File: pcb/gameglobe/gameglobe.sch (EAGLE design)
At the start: 14 parts

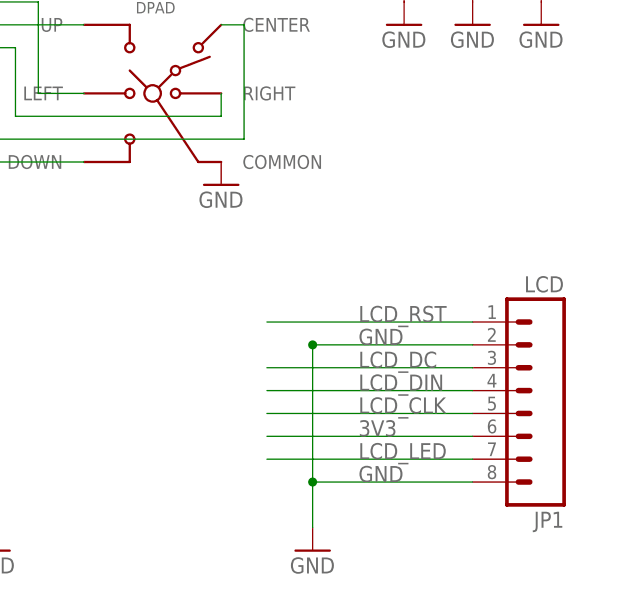
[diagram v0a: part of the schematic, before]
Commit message: Improved silkscreen
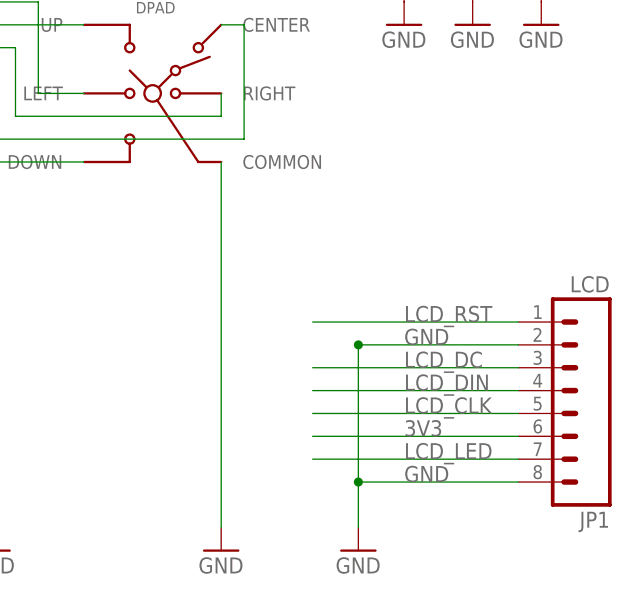
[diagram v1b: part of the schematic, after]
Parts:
- JP1: device SparkFun-Connectors:M08NO_SILK -> SparkFun-Connectors:M08
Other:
- moved on the sheet: JP1
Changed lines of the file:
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@@
 <part name="GND1" library="supply1" deviceset="GND" device=""/>
 <part name="GND2" library="supply1" deviceset="GND" device=""/>
-<part name="JP1" library="SparkFun-Connectors" deviceset="M08" device="NO_SILK" value="LCD"/>
+<part name="JP1" library="SparkFun-Connectors" deviceset="M08" device="" value="LCD"/>
 <part name="GND3" library="supply1" deviceset="GND" device=""/>
 <part name="GND4" library="supply1" deviceset="GND" device=""/>
@@
 <instance part="GND1" gate="1" x="96.52" y="0"/>
 <instance part="GND2" gate="1" x="15.24" y="0"/>
-<instance part="JP1" gate="G$1" x="154.94" y="17.78" rot="R180"/>
-<instance part="GND3" gate="1" x="132.08" y="0"/>
+<instance part="JP1" gate="G$1" x="160.02" y="17.78" rot="R180"/>
+<instance part="GND3" gate="1" x="137.16" y="0"/>
 <instance part="GND4" gate="1" x="15.24" y="58.42"/>
 <instance part="GND5" gate="1" x="142.24" y="58.42"/>
@@
 <instance part="GND7" gate="1" x="157.48" y="58.42"/>
 <instance part="DPAD" gate="Q$1" x="114.3" y="50.8"/>
-<instance part="GND8" gate="1" x="121.92" y="40.64"/>
+<instance part="GND8" gate="1" x="121.92" y="0"/>
 <instance part="R1" gate="G$1" x="20.32" y="30.48"/>
 <instance part="ARDUINO_NANO" gate="G$1" x="66.04" y="12.7" rot="R180"/>
@@
 </segment>
 <segment>
-<wire x1="132.08" y1="22.86" x2="132.08" y2="7.62" width="0.1524" layer="91"/>
+<wire x1="137.16" y1="22.86" x2="137.16" y2="7.62" width="0.1524" layer="91"/>
 <pinref part="JP1" gate="G$1" pin="8"/>
-<wire x1="149.86" y1="7.62" x2="132.08" y2="7.62" width="0.1524" layer="91"/>
-<label x="137.16" y="7.62" size="1.778" layer="95"/>
+<wire x1="154.94" y1="7.62" x2="137.16" y2="7.62" width="0.1524" layer="91"/>
+<label x="142.24" y="7.62" size="1.778" layer="95"/>
 <pinref part="JP1" gate="G$1" pin="2"/>
-<wire x1="149.86" y1="22.86" x2="132.08" y2="22.86" width="0.1524" layer="91"/>
-<label x="137.16" y="22.86" size="1.778" layer="95"/>
-<junction x="132.08" y="22.86"/>
+<wire x1="154.94" y1="22.86" x2="137.16" y2="22.86" width="0.1524" layer="91"/>
+<label x="142.24" y="22.86" size="1.778" layer="95"/>
+<junction x="137.16" y="22.86"/>
 <pinref part="GND3" gate="1" pin="GND"/>
-<wire x1="132.08" y1="7.62" x2="132.08" y2="2.54" width="0.1524" layer="91"/>
-<junction x="132.08" y="7.62"/>
+<wire x1="137.16" y1="7.62" x2="137.16" y2="2.54" width="0.1524" layer="91"/>
+<junction x="137.16" y="7.62"/>
 </segment>
 <segment>
@@
 <pinref part="DPAD" gate="Q$1" pin="COMMON"/>
 <pinref part="GND8" gate="1" pin="GND"/>
+<wire x1="121.92" y1="2.54" x2="121.92" y2="43.18" width="0.1524" layer="91"/>
 </segment>
 </net>
@@
 <segment>
 <pinref part="JP1" gate="G$1" pin="1"/>
-<wire x1="149.86" y1="25.4" x2="127" y2="25.4" width="0.1524" layer="91"/>
-<label x="137.16" y="25.4" size="1.778" layer="95"/>
+<wire x1="154.94" y1="25.4" x2="132.08" y2="25.4" width="0.1524" layer="91"/>
+<label x="142.24" y="25.4" size="1.778" layer="95"/>
 </segment>
 <segment>
@@
 <segment>
 <pinref part="JP1" gate="G$1" pin="3"/>
-<wire x1="149.86" y1="20.32" x2="127" y2="20.32" width="0.1524" layer="91"/>
-<label x="137.16" y="20.32" size="1.778" layer="95"/>
+<wire x1="154.94" y1="20.32" x2="132.08" y2="20.32" width="0.1524" layer="91"/>
+<label x="142.24" y="20.32" size="1.778" layer="95"/>
 </segment>
 <segment>
@@
 <segment>
 <pinref part="JP1" gate="G$1" pin="4"/>
-<wire x1="149.86" y1="17.78" x2="127" y2="17.78" width="0.1524" layer="91"/>
-<label x="137.16" y="17.78" size="1.778" layer="95"/>
+<wire x1="154.94" y1="17.78" x2="132.08" y2="17.78" width="0.1524" layer="91"/>
+<label x="142.24" y="17.78" size="1.778" layer="95"/>
 </segment>
 <segment>
@@
 <segment>
 <pinref part="JP1" gate="G$1" pin="5"/>
-<wire x1="149.86" y1="15.24" x2="127" y2="15.24" width="0.1524" layer="91"/>
-<label x="137.16" y="15.24" size="1.778" layer="95"/>
+<wire x1="154.94" y1="15.24" x2="132.08" y2="15.24" width="0.1524" layer="91"/>
+<label x="142.24" y="15.24" size="1.778" layer="95"/>
 </segment>
 <segment>
@@
 <segment>
 <pinref part="JP1" gate="G$1" pin="6"/>
-<wire x1="149.86" y1="12.7" x2="127" y2="12.7" width="0.1524" layer="91"/>
-<label x="137.16" y="12.7" size="1.778" layer="95"/>
+<wire x1="154.94" y1="12.7" x2="132.08" y2="12.7" width="0.1524" layer="91"/>
+<label x="142.24" y="12.7" size="1.778" layer="95"/>
 </segment>
 <segment>
@@
 <segment>
 <pinref part="JP1" gate="G$1" pin="7"/>
-<wire x1="149.86" y1="10.16" x2="127" y2="10.16" width="0.1524" layer="91"/>
-<label x="137.16" y="10.16" size="1.778" layer="95"/>
+<wire x1="154.94" y1="10.16" x2="132.08" y2="10.16" width="0.1524" layer="91"/>
+<label x="142.24" y="10.16" size="1.778" layer="95"/>
 </segment>
 <segment>

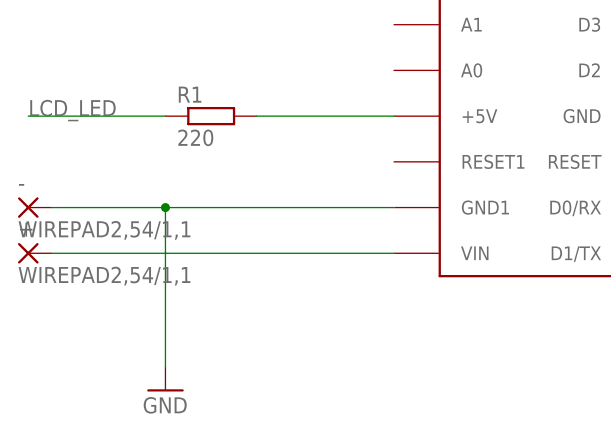
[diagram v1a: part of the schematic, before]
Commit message: Added power switch to pcb. LCD pin labels on slikscreen
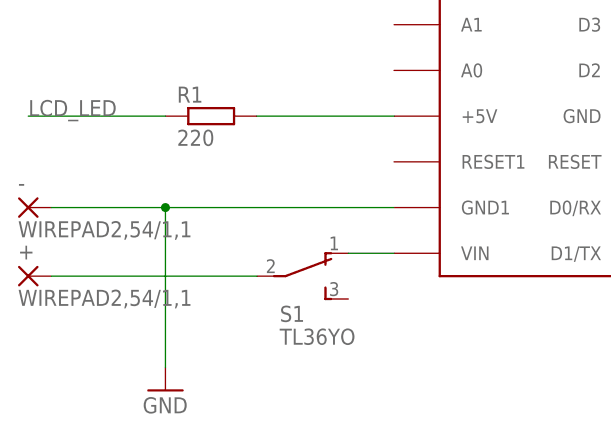
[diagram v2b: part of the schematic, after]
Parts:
- added S1: TL36YO, switch:TL36YO
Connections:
- removed net N$7: +.P, ARDUINO_NANO.VIN
- new net N$5: ARDUINO_NANO.VIN, S1.O
- new net N$6: +.P, S1.P
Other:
- moved on the sheet: +
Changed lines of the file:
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@@
 <part name="R1" library="resistor" deviceset="R-EU_" device="0411/15" value="220"/>
 <part name="ARDUINO_NANO" library="arduino_nano" deviceset="ARDUINONANO" device=""/>
+<part name="S1" library="switch" deviceset="TL36YO" device=""/>
 </parts>
 <sheets>
@@
 </plain>
 <instances>
-<instance part="+" gate="G$1" x="0" y="15.24"/>
+<instance part="+" gate="G$1" x="0" y="12.7"/>
 <instance part="-" gate="G$1" x="0" y="20.32"/>
 <instance part="R5" gate="G$1" x="22.86" y="86.36"/>
@@
 <instance part="R1" gate="G$1" x="20.32" y="30.48"/>
 <instance part="ARDUINO_NANO" gate="G$1" x="66.04" y="12.7" rot="R180"/>
+<instance part="S1" gate="BEF1" x="30.48" y="12.7" rot="R270"/>
 </instances>
 <busses>
 </busses>
 <nets>
-<net name="N$7" class="0">
-<segment>
-<pinref part="+" gate="G$1" pin="P"/>
-<wire x1="40.64" y1="15.24" x2="2.54" y2="15.24" width="0.1524" layer="91"/>
-<pinref part="ARDUINO_NANO" gate="G$1" pin="VIN"/>
-</segment>
-</net>
 <net name="GND" class="0">
 <segment>
@@
 </segment>
 </net>
+<net name="N$5" class="0">
+<segment>
+<pinref part="ARDUINO_NANO" gate="G$1" pin="VIN"/>
+<pinref part="S1" gate="BEF1" pin="O"/>
+<wire x1="40.64" y1="15.24" x2="35.56" y2="15.24" width="0.1524" layer="91"/>
+</segment>
+</net>
+<net name="N$6" class="0">
+<segment>
+<pinref part="S1" gate="BEF1" pin="P"/>
+<pinref part="+" gate="G$1" pin="P"/>
+<wire x1="25.4" y1="12.7" x2="2.54" y2="12.7" width="0.1524" layer="91"/>
+</segment>
+</net>

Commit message: Set LED resistor value to 100 (after testing with prototype); Move some silkscreen items around; Enable all needed layers in Eagle
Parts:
- R1: value 220 -> 100
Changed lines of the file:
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@@
 <part name="DPAD" library="gamaral" deviceset="SKQU" device="CAA010"/>
 <part name="GND8" library="supply1" deviceset="GND" device=""/>
-<part name="R1" library="resistor" deviceset="R-EU_" device="0411/15" value="220"/>
+<part name="R1" library="resistor" deviceset="R-EU_" device="0411/15" value="100"/>
 <part name="ARDUINO_NANO" library="arduino_nano" deviceset="ARDUINONANO" device=""/>
 <part name="S1" library="switch" deviceset="TL36YO" device=""/>

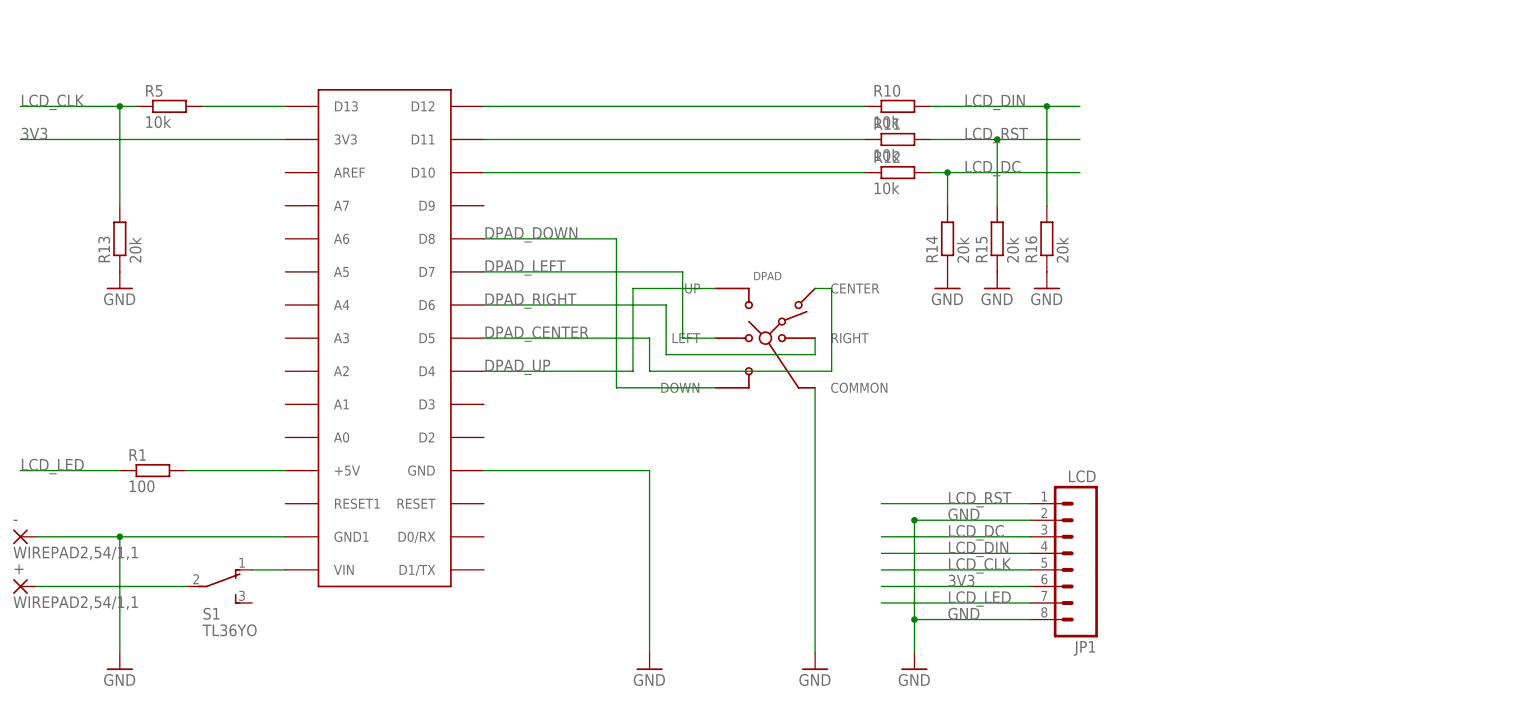
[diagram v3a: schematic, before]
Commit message: Changed to cheaper speaker (flat piezo buzzer); Mount speaker belof display, add connector for speaker; Improve 9V connector; Improve silkscreen again;
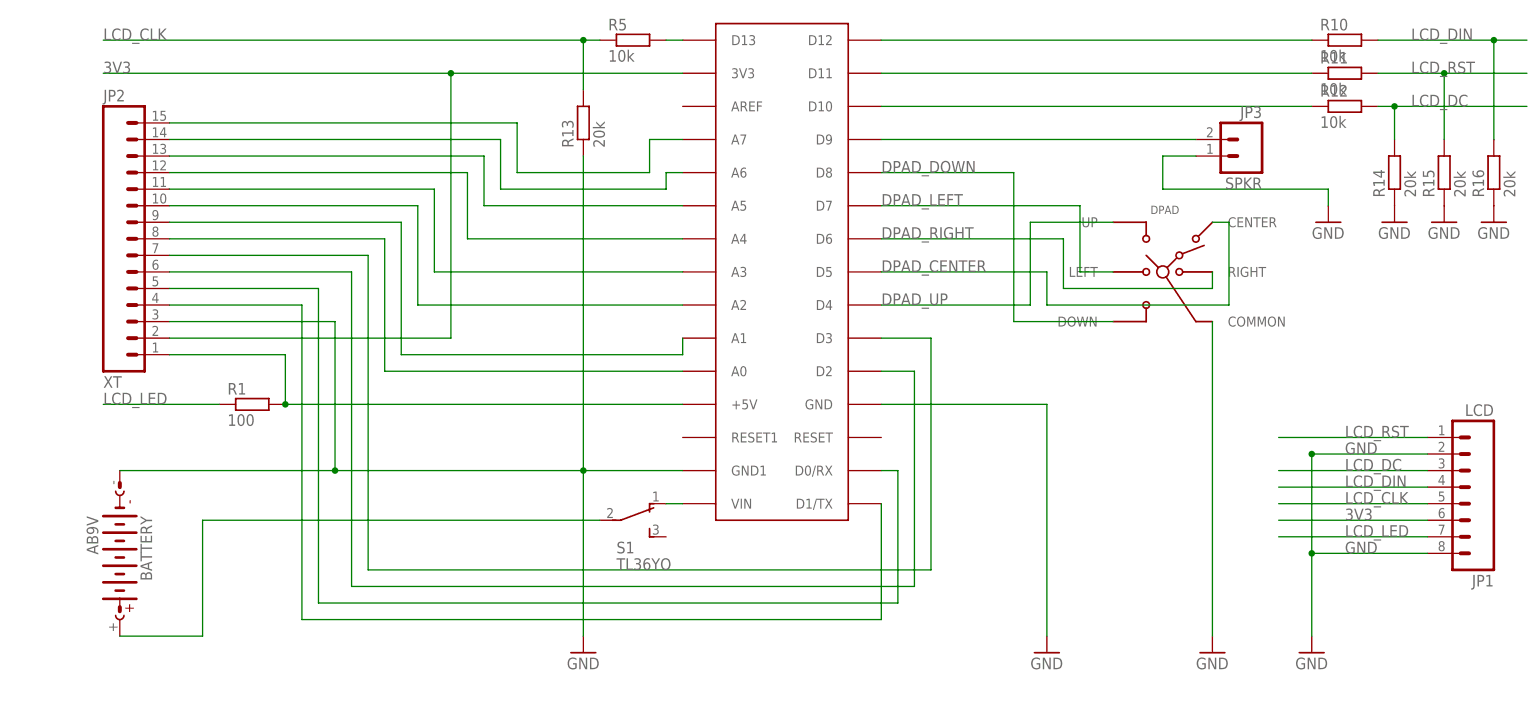
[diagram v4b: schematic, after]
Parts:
- removed +, -: WIREPAD2,54/1,1, wirepad:WIREPAD2,54/1,1
- added BATTERY: AB9V, battery:AB9V
- added JP2: XT, SparkFun-Connectors:M15
- added JP3: SPKR, SparkFun-Connectors:M02PTH
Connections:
- new net N$11: ARDUINO_NANO.A0, JP2.8
- new net N$12: ARDUINO_NANO.A1, JP2.9
- new net N$13: ARDUINO_NANO.A2, JP2.10
- new net N$14: ARDUINO_NANO.A3, JP2.11
- new net N$15: ARDUINO_NANO.A4, JP2.12
- new net N$16: ARDUINO_NANO.A5, JP2.13
- new net N$17: ARDUINO_NANO.A6, JP2.14
- new net N$18: ARDUINO_NANO.A7, JP2.15
- new net N$19: ARDUINO_NANO.D3, JP2.7
- new net N$7: ARDUINO_NANO.D1/TX, JP2.4
- new net N$8: ARDUINO_NANO.D0/RX, JP2.5
- new net N$9: ARDUINO_NANO.D2, JP2.6
- new net SPKR: ARDUINO_NANO.D9, JP3.2
- net 3V3: now also JP2.2
- net 5V: now also JP2.1
- net GND: now also BATTERY.-, JP2.3, JP3.1; no longer -.P
- net N$6: now also BATTERY.+; no longer +.P
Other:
- moved on the sheet: DPAD, JP1, R1, R10, R11, R12, R13, R14, R15, R16, R5, S1

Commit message: change wiring to use different pins for the speaker with ToneAC library (and also all the buttons)
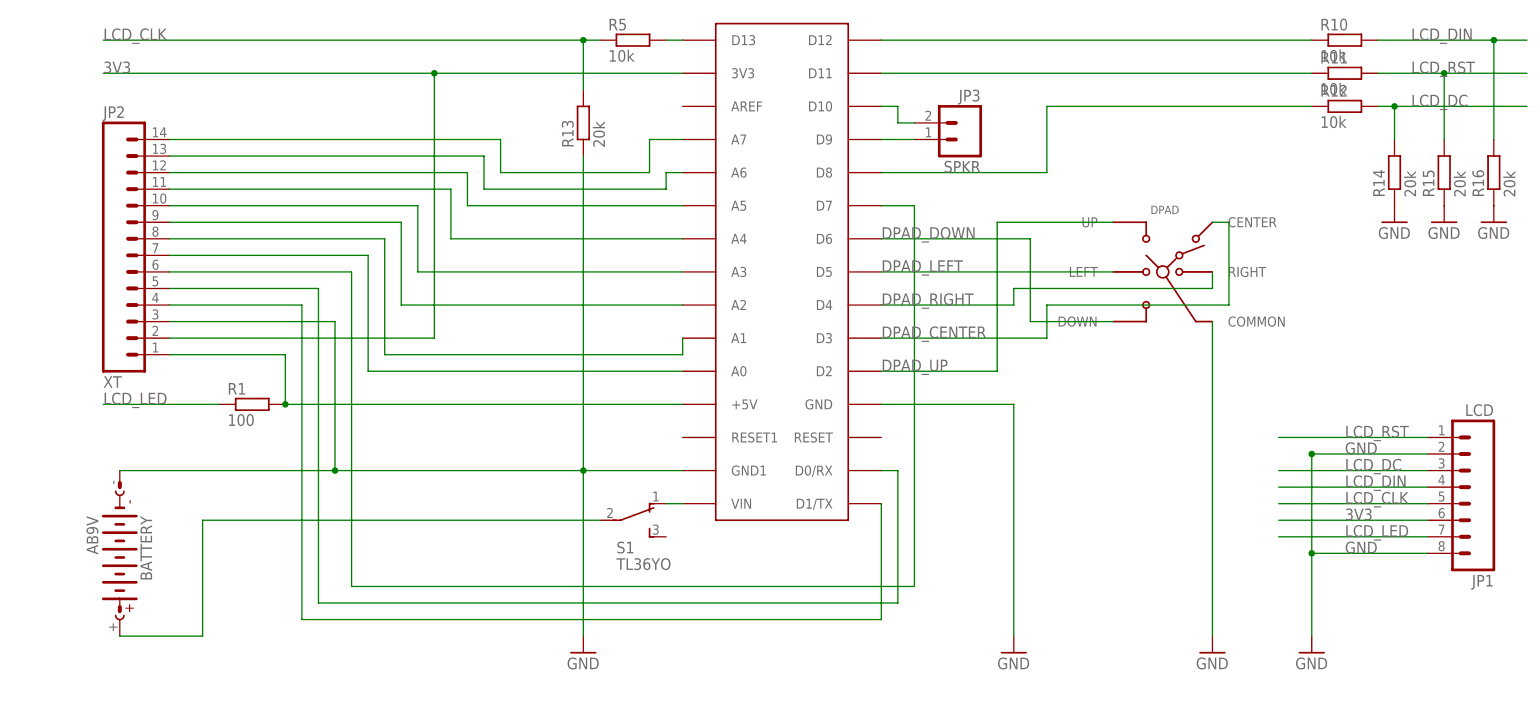
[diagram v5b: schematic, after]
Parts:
- JP2: device SparkFun-Connectors:M15 -> SparkFun-Connectors:M14LONGPADS
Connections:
- removed net N$19: ARDUINO_NANO.D3, JP2.7
- removed net SPKR: ARDUINO_NANO.D9, JP3.2
- new net N$10: ARDUINO_NANO.D10, JP3.2
- new net N$20: ARDUINO_NANO.D8, R12.1
- net DPAD_CENTER: now also ARDUINO_NANO.D3; no longer ARDUINO_NANO.D5
- net DPAD_DOWN: now also ARDUINO_NANO.D6; no longer ARDUINO_NANO.D8
- net DPAD_LEFT: now also ARDUINO_NANO.D5; no longer ARDUINO_NANO.D7
- net DPAD_RIGHT: now also ARDUINO_NANO.D4; no longer ARDUINO_NANO.D6
- net DPAD_UP: now also ARDUINO_NANO.D2; no longer ARDUINO_NANO.D4
- net GND: no longer JP3.1
- net N$11: now also JP2.7; no longer JP2.8
- net N$12: now also JP2.8; no longer JP2.9
- net N$13: now also JP2.9; no longer JP2.10
- net N$14: now also JP2.10; no longer JP2.11
- net N$15: now also JP2.11; no longer JP2.12
- net N$16: now also JP2.12; no longer JP2.13
- net N$17: now also JP2.13; no longer JP2.14
- net N$18: now also JP2.14; no longer JP2.15
- net N$4: now also ARDUINO_NANO.D9, JP3.1; no longer ARDUINO_NANO.D10, R12.1
- net N$9: now also ARDUINO_NANO.D7; no longer ARDUINO_NANO.D2
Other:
- moved on the sheet: JP3

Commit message: change pin numbers (just as in the code, see previous commit), also use ground plane
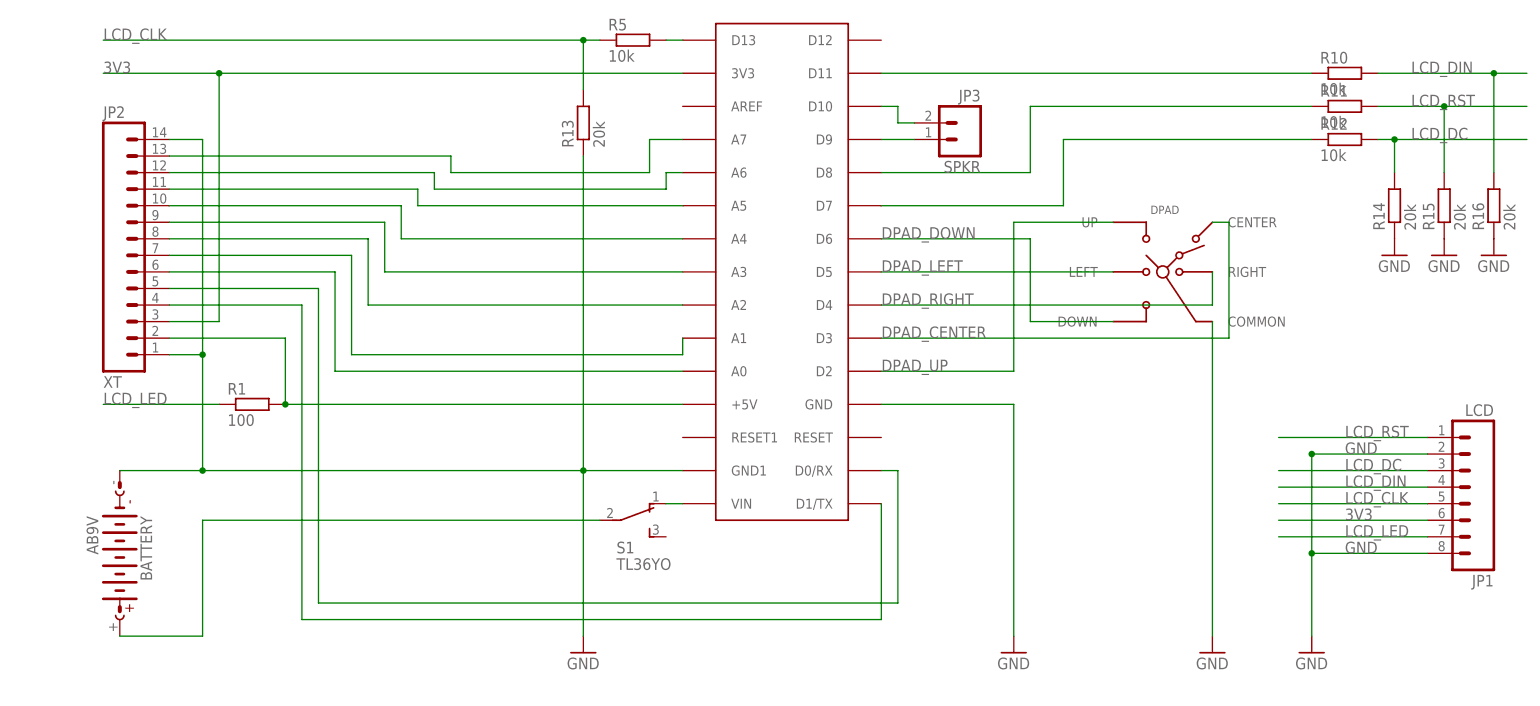
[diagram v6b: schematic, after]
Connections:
- removed net N$9: ARDUINO_NANO.D7, JP2.6
- net 3V3: now also JP2.3; no longer JP2.2
- net 5V: now also JP2.2; no longer JP2.1
- net GND: now also JP2.1, JP2.14; no longer JP2.3
- net N$11: now also JP2.6; no longer JP2.7
- net N$12: now also JP2.7; no longer JP2.8
- net N$13: now also JP2.8; no longer JP2.9
- net N$14: now also JP2.9; no longer JP2.10
- net N$15: now also JP2.10; no longer JP2.11
- net N$16: now also JP2.11; no longer JP2.12
- net N$17: now also JP2.12; no longer JP2.13
- net N$18: now also JP2.13; no longer JP2.14
- net N$2: now also ARDUINO_NANO.D11; no longer ARDUINO_NANO.D12
- net N$20: now also ARDUINO_NANO.D7; no longer ARDUINO_NANO.D8
- net N$3: now also ARDUINO_NANO.D8; no longer ARDUINO_NANO.D11
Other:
- moved on the sheet: R10, R11, R12, R14, R15, R16
